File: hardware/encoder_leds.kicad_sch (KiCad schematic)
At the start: 68 parts, among them U7 MAX7219

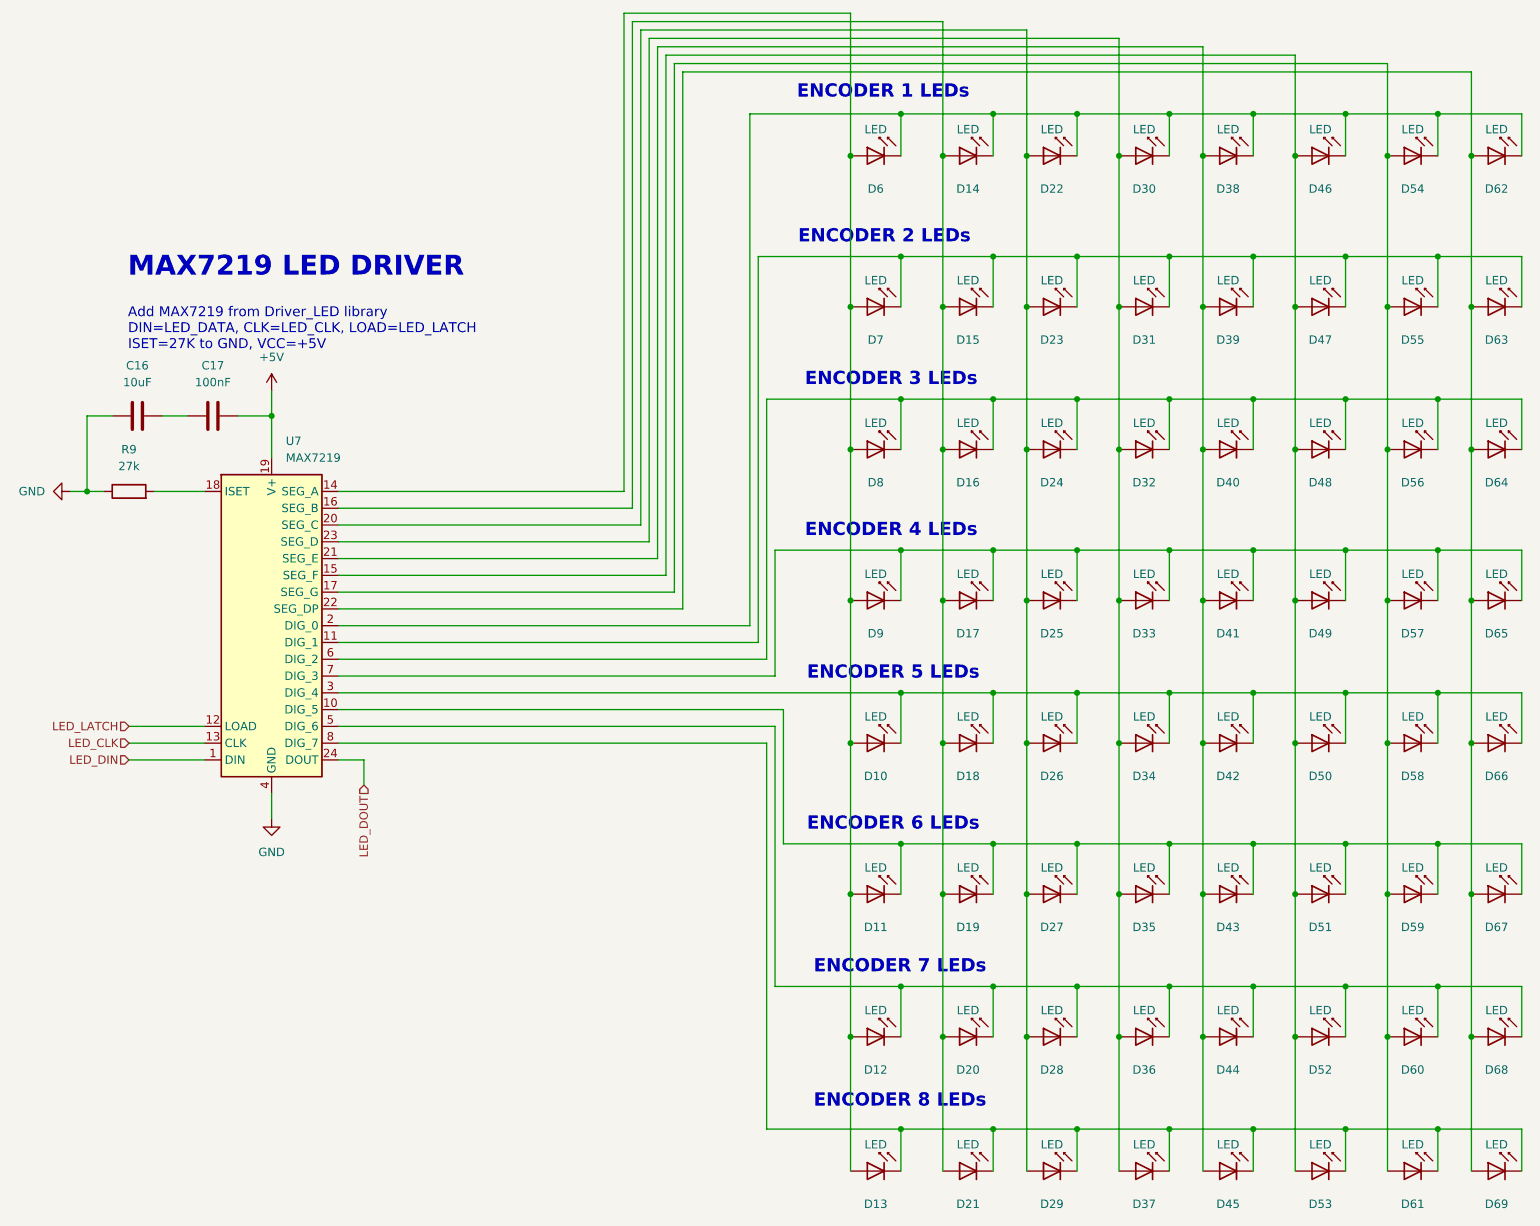
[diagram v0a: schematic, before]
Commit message: Complete hierarchical schematic sheets and fix wiring
- Complete encoder_leds sheet with MAX7219 + 64 LEDs
- Complete ui_leds sheet with MAX7219 + 45 LEDs
- Complete buttons sheet with MCP23017 + 40 buttons
- Complete display sheet with OLED I2C connector
- Complete pots sheet with 3 potentiometers
- Complete encoders sheet with 8 rotary encoders on MCP23017
- Fix inputs sheet hierarchical labels (CLK_IN, RST_IN, SCENE_CV_IN)
- Update MCU sheet with ADC hierarchical labels
- Update root sheet with hierarchical pin connections
- Various ERC fixes and wiring corrections

Co-Authored-By: Claude Opus 4.5 <noreply@anthropic.com>
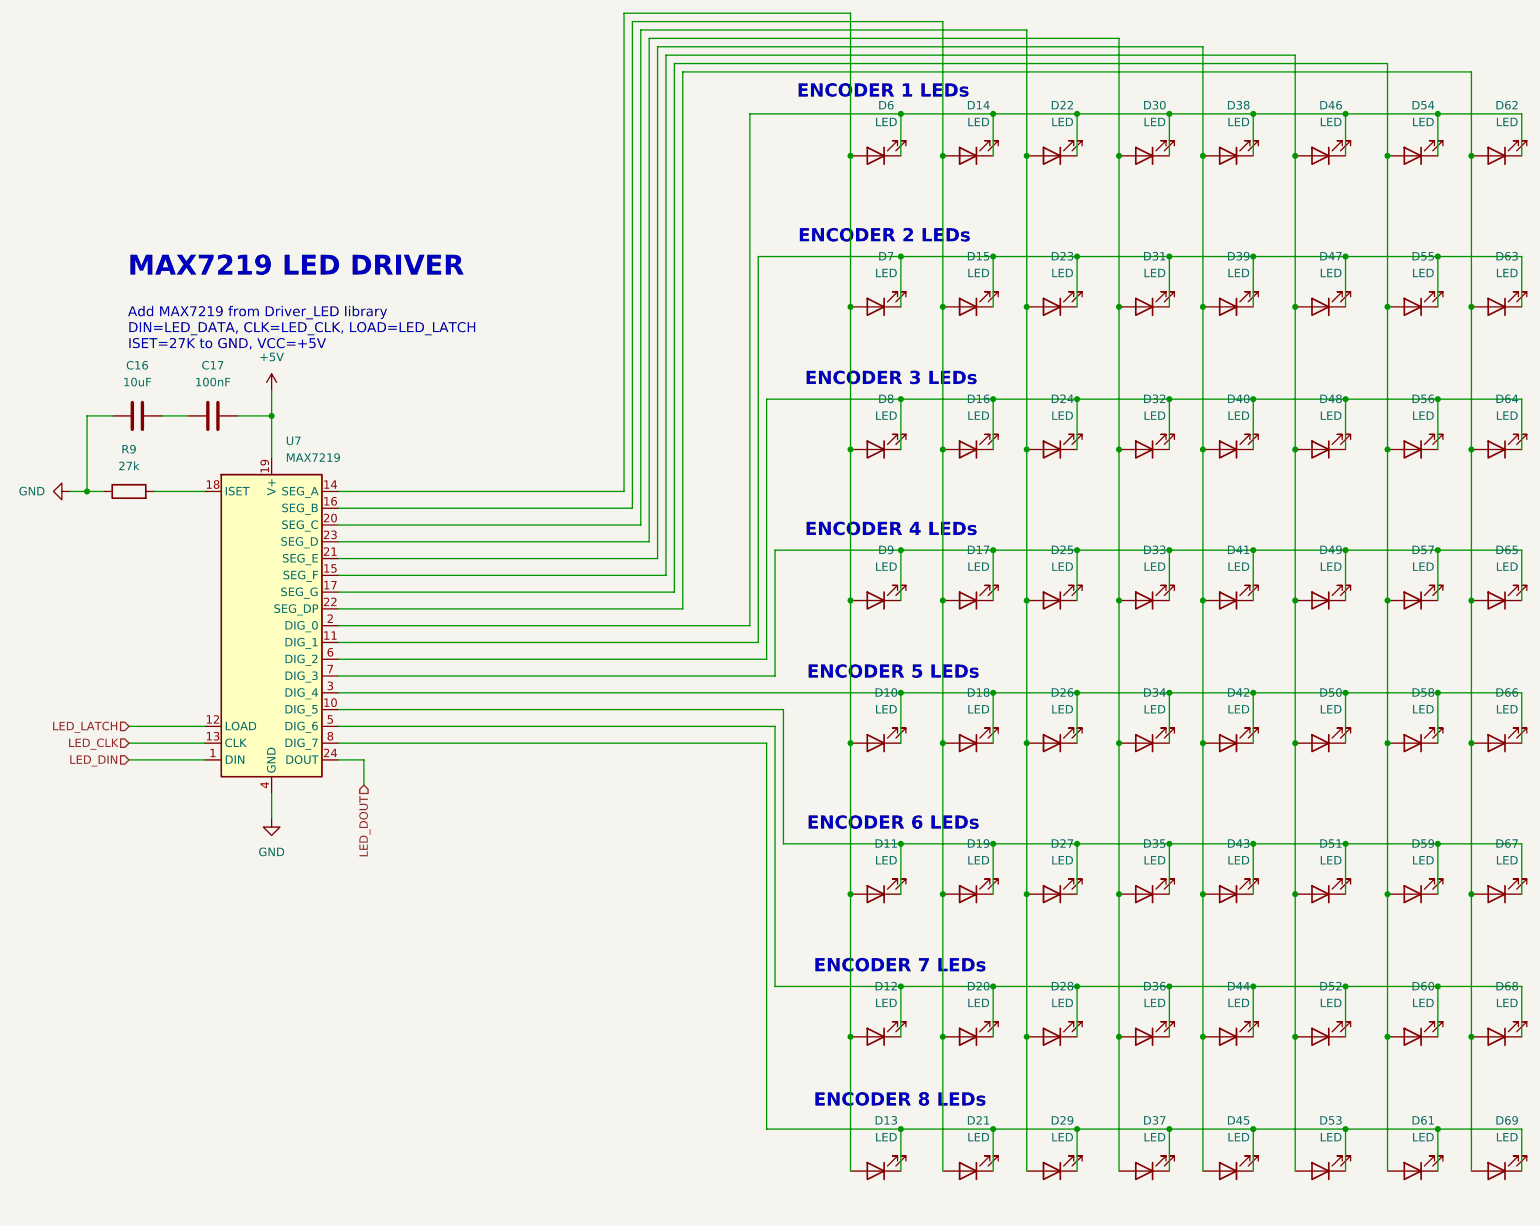
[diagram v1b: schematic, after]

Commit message: Assign footprints to all schematic components
SMD footprints assigned:
- Capacitors: 0402 (20pF), 0603 (100nF), 0805 (10uF), 1206 (47uF, 100uF)
- Resistors: 0603
- LEDs: 0201
- MAX7219: SOIC-24W
- ULN2003: SOIC-16
- Switches: TL3342 tactile
- Connectors: JST PH, pin headers

Also removes accidentally committed autosave files.

Co-Authored-By: Claude Opus 4.5 <noreply@anthropic.com>
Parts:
- C16: footprint (none) -> Capacitor_SMD:C_0805_2012Metric
- C17: footprint (none) -> Capacitor_SMD:C_0603_1608Metric
- R9: footprint (none) -> Resistor_SMD:R_0201_0603Metric_Pad0.64x0.40mm_HandSolder
- U7: footprint (none) -> Package_SO:SOIC-24W_7.5x15.4mm_P1.27mm
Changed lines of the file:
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@@
 			)
 		)
-		(property "Footprint" ""
+		(property "Footprint" "Capacitor_SMD:C_0603_1608Metric"
 			(at 102.87 110.7948 0)
 			(effects
@@
 			)
 		)
-		(property "Footprint" ""
+		(property "Footprint" "Resistor_SMD:R_0201_0603Metric_Pad0.64x0.40mm_HandSolder"
 			(at 86.36 124.968 90)
 			(effects
@@
 			)
 		)
-		(property "Footprint" ""
+		(property "Footprint" "Package_SO:SOIC-24W_7.5x15.4mm_P1.27mm"
 			(at 106.68 142.24 0)
 			(effects
@@
 			)
 		)
-		(property "Footprint" ""
+		(property "Footprint" "Capacitor_SMD:C_0805_2012Metric"
 			(at 91.44 110.7948 0)
 			(effects
